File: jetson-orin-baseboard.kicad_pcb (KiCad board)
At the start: 2 copper layers, 0 parts

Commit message: Add basic mechanical outline
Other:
- board outline added: 110 x 55 mm
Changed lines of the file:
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@@
   )
   (net 0 "")
+  (gr_rect (start 20 20) (end 130 75) (layer "Edge.Cuts") (width 0.1) (fill none))
 )

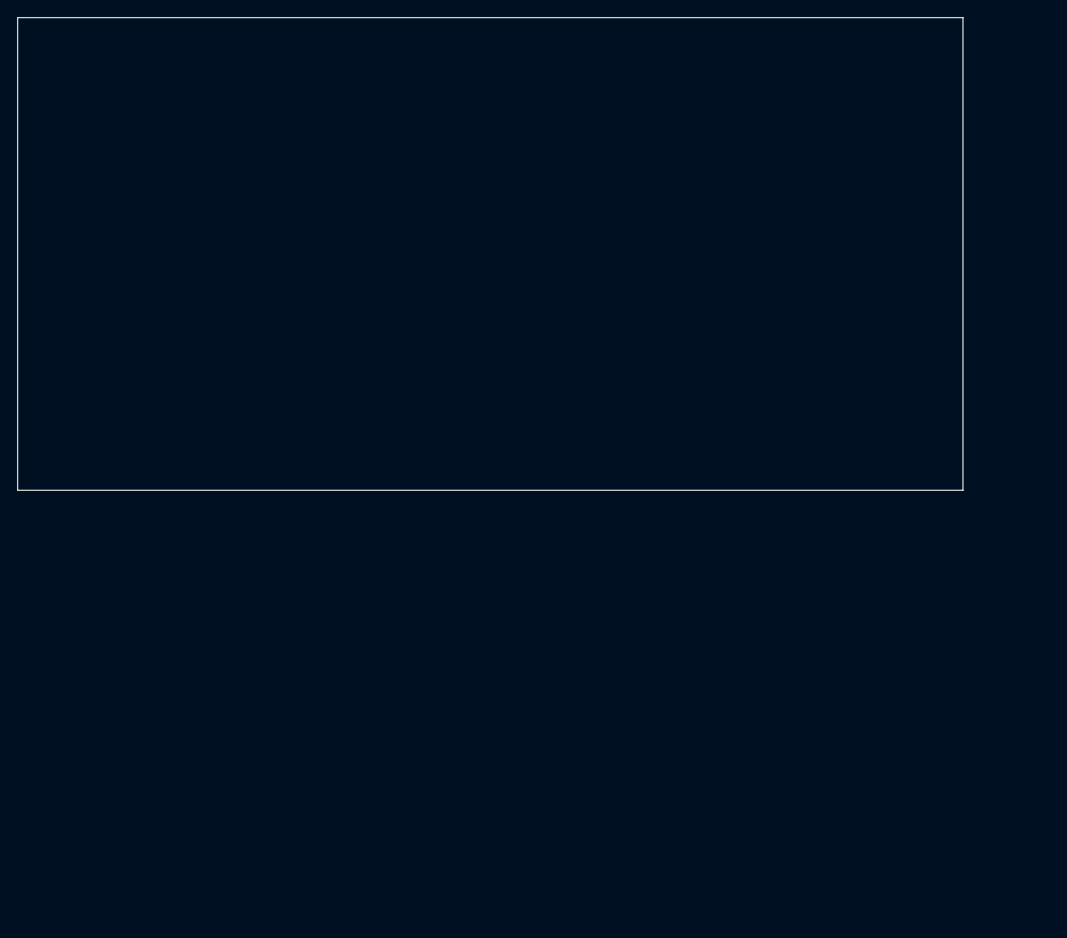
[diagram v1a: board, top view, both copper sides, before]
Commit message: Setup stackup and add stackup table
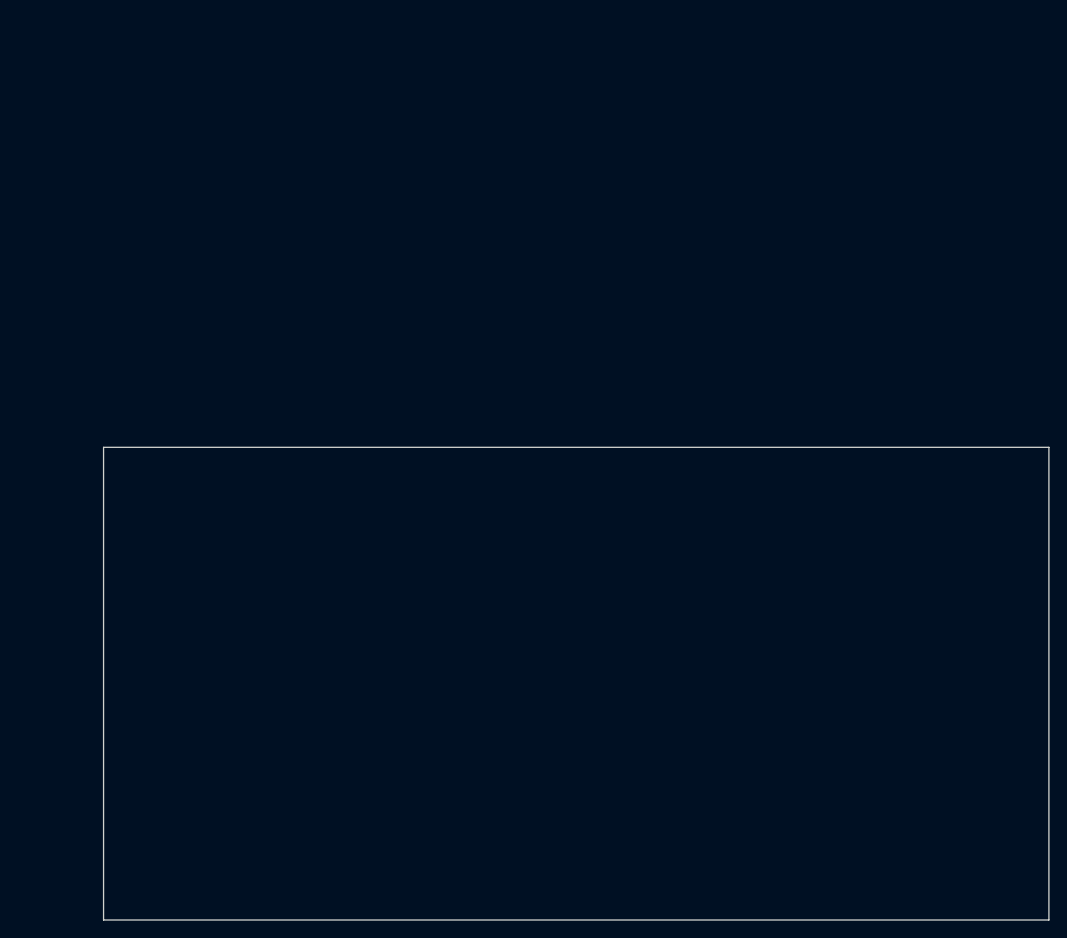
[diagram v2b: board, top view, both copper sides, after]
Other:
- copper layers 2 -> 8
- board text added: "0"
- board text added: "0 mm"
- board text added: "0.01 mm"
- board text added: "0.02"
- board text added: "0.035 mm"
- board text added: "0.12 mm"
- board text added: "0.2 mm"
- board text added: "1"
- board text added: "3.3"
- board text added: "4.3"
- board text added: "4.39"
- board text added: "B.Cu"
- board text added: "B.Mask"
- board text added: "B.Paste"
- board text added: "B.Silkscreen"
- board text added: "Black"
- board text added: "Bottom Silk Screen"
- board text added: "Bottom Solder Mask"
- board text added: "Bottom Solder Paste"
- board text added: "Color"
- board text added: "Dielectric 1"
- board text added: "Dielectric 2"
- board text added: "Dielectric 3 (1/2)"
- board text added: "Dielectric 4"
- board text added: "Dielectric 5 (1/2)"
- board text added: "Dielectric 6"
- board text added: "Dielectric 7"
- board text added: "Epsilon R"
- board text added: "F.Cu"
- board text added: "F.Mask"
- board text added: "F.Paste"
- board text added: "F.Silkscreen"
- board text added: "FR4"
- board text added: "In1.Cu"
- board text added: "In2.Cu"
- board text added: "In3.Cu"
- board text added: "In4.Cu"
- board text added: "In5.Cu"
- board text added: "In6.Cu"
- board text added: "Layer Name"
- board text added: "Loss Tangent"
- board text added: "Material"
- board text added: "Not specified"
- board text added: "PR2116"
- board text added: "Thickness (mm)"
- board text added: "Top Silk Screen"
- board text added: "Top Solder Mask"
- board text added: "Top Solder Paste"
- board text added: "Type"
- board text added: "White"
- board text added: "copper"
- board text added: "core"
- board text added: "prepreg"

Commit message: Initial mechanical arrangement
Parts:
- added BAT201: MS621FE-FL11E, antmicro-footprints:MS621FE-FL11E, F.Cu at (-236.6, 36.6)
- added C201: C_22u_0805_25V, antmicro-footprints:0805-cap, F.Cu at (-316.6, 80.5)
- added C202: C_22u_0805_25V, antmicro-footprints:0805-cap, F.Cu at (-230.2, 29.0)
- added C203: C_22u_0805_25V, antmicro-footprints:0805-cap, F.Cu at (-304.9, 77.2)
- added C204: C_22u_0805_25V, antmicro-footprints:0805-cap, F.Cu at (-316.6, 83.5)
- added C205: C_100n_0402, antmicro-footprints:0402-cap, F.Cu at (-226.3, 28.5)
- added C301: C_10u_0603, antmicro-footprints:0603-cap, F.Cu at (-266.7, 96.3)
- added C302: C_10u_0603, antmicro-footprints:0603-cap, F.Cu at (-270.6, 98.7)
- added C303: C_10u_0603, antmicro-footprints:0603-cap, F.Cu at (-258.5, 89.3)
- added C304: C_10u_0603, antmicro-footprints:0603-cap, F.Cu at (-317.2, 181.8)
- added C305: C_100n_0402, antmicro-footprints:0402-cap, F.Cu at (-258.8, 91.5)
- added C306: C_100n_0402, antmicro-footprints:0402-cap, F.Cu at (-249.4, 89.0)
- added C307: C_100n_0402, antmicro-footprints:0402-cap, F.Cu at (-260.6, 94.1)
- added C308: C_100n_0402, antmicro-footprints:0402-cap, F.Cu at (-270.9, 109.4)
- added C309: C_100n_0402, antmicro-footprints:0402-cap, F.Cu at (-268.0, 106.9)
- added C310: C_100n_0402, antmicro-footprints:0402-cap, F.Cu at (-267.3, 103.0)
- added C311: C_100n_0402, antmicro-footprints:0402-cap, F.Cu at (-263.5, 94.1)
- added C312: C_100n_0402, antmicro-footprints:0402-cap, F.Cu at (-263.5, 96.1)
- added C313: C_100n_0402, antmicro-footprints:0402-cap, F.Cu at (-263.5, 98.1)
- added C318: C_100n_0402, antmicro-footprints:0402-cap, F.Cu at (-270.9, 105.4)
- added C323: C_10u_0603, antmicro-footprints:0603-cap, F.Cu at (-267.0, 98.7)
- added C324: C_10u_0603, antmicro-footprints:0603-cap, F.Cu at (-270.6, 101.2)
- added C401: C_100n_0402, antmicro-footprints:0402-cap, F.Cu at (-128.9, 68.3)
- added C402: C_10u_0603, antmicro-footprints:0603-cap, F.Cu at (-103.0, 31.2)
- added C405: C_10u_0603, antmicro-footprints:0603-cap, F.Cu at (-120.6, 46.8)
- added C412: C_100n_0402, antmicro-footprints:0402-cap, F.Cu at (-110.9, 49.1)
- added C413: C_100n_0402, antmicro-footprints:0402-cap, F.Cu at (-104.7, 41.6)
- added C414: C_100n_0402, antmicro-footprints:0402-cap, F.Cu at (-95.2, 37.0)
- added C415: C_100n_0402, antmicro-footprints:0402-cap, F.Cu at (-117.3, 49.0)
- added C416: C_100n_0402, antmicro-footprints:0402-cap, F.Cu at (-104.5, 33.5)
- added C417: C_100n_0402, antmicro-footprints:0402-cap, F.Cu at (-107.8, 45.6)
- added C418: C_100n_0402, antmicro-footprints:0402-cap, F.Cu at (-87.2, 28.5)
- added C419: C_100n_0402, antmicro-footprints:0402-cap, F.Cu at (-98.1, 35.0)
- added C420: C_100n_0402, antmicro-footprints:0402-cap, F.Cu at (-96.8, 31.0)
- added C421: C_100n_0402, antmicro-footprints:0402-cap, F.Cu at (-111.6, 51.0)
- added C422: C_100n_0402, antmicro-footprints:0402-cap, F.Cu at (-121.8, 56.8)
- added C423: C_100n_0402, antmicro-footprints:0402-cap, F.Cu at (-95.7, 33.0)
- added C424: C_100n_0402, antmicro-footprints:0402-cap, F.Cu at (-99.7, 31.0)
- added C425: C_100n_0402, antmicro-footprints:0402-cap, F.Cu at (-125.4, 62.7)
- added C426: C_100n_0402, antmicro-footprints:0402-cap, F.Cu at (-113.6, 46.0)
- added C427: C_100n_0402, antmicro-footprints:0402-cap, F.Cu at (-128.3, 62.4)
- added C428: C_100n_0402, antmicro-footprints:0402-cap, F.Cu at (-107.8, 47.6)
- added C429: C_100n_0402, antmicro-footprints:0402-cap, F.Cu at (-131.8, 66.0)
- added C430: C_100n_0402, antmicro-footprints:0402-cap, F.Cu at (-90.1, 28.5)
- added C431: C_100n_0402, antmicro-footprints:0402-cap, F.Cu at (-125.4, 60.8)
- added C432: C_100n_0402, antmicro-footprints:0402-cap, F.Cu at (-123.1, 64.7)
- added C433: C_100n_0402, antmicro-footprints:0402-cap, F.Cu at (-93.0, 28.5)
- added C434: C_10u_25V_0603, antmicro-footprints:0603-cap, F.Cu at (-120.6, 49.2)
- added C435: C_10u_0402, antmicro-footprints:0402-cap, F.Cu at (-101.0, 35.5)
- added C436: C_10u_0402, antmicro-footprints:0402-cap, F.Cu at (-117.4, 53.5)
- added C437: C_10u_0402, antmicro-footprints:0402-cap, F.Cu at (-98.9, 41.4)
- added C438: C_10u_0402, antmicro-footprints:0402-cap, F.Cu at (-98.8, 39.4)
- added C439: C_100n_0402, antmicro-footprints:0402-cap, F.Cu at (-110.7, 43.1)
- added C440: C_100n_0402, antmicro-footprints:0402-cap, F.Cu at (-118.9, 55.4)
- added C441: C_100n_0402, antmicro-footprints:0402-cap, F.Cu at (-101.6, 33.5)
- added C442: C_100n_0402, antmicro-footprints:0402-cap, F.Cu at (-128.3, 60.4)
- added C443: C_100n_0402_50V, antmicro-footprints:0402-cap, F.Cu at (-98.1, 37.0)
- added C444: C_100n_0402_50V, antmicro-footprints:0402-cap, F.Cu at (-101.7, 39.4)
- added C501: C_10u_0603, antmicro-footprints:0603-cap, F.Cu at (-32.5, 36.9)
- added C503: C_100n_0402, antmicro-footprints:0402-cap, F.Cu at (-21.7, 40.9)
- added C505: C_100n_0402, antmicro-footprints:0402-cap, F.Cu at (-21.9, 31.0)
- added C507: C_100n_0402, antmicro-footprints:0402-cap, F.Cu at (-33.4, 41.7)
- added C508: C_100n_0402, antmicro-footprints:0402-cap, F.Cu at (-22.8, 37.0)
- added C511: C_100n_0402, antmicro-footprints:0402-cap, F.Cu at (-21.7, 42.9)
- added C512: C_100n_0402, antmicro-footprints:0402-cap, F.Cu at (-10.3, 32.5)
- added C515: C_100n_0402, antmicro-footprints:0402-cap, F.Cu at (-38.0, 52.4)
- added C517: C_10u_0603, antmicro-footprints:0603-cap, F.Cu at (-47.1, 52.4)
- added C519: C_100n_0402, antmicro-footprints:0402-cap, F.Cu at (-24.6, 43.1)
- added C601: C_100n_0805_100V, antmicro-footprints:0805-cap, F.Cu at (-175.4, 50.0)
- added C602: C_10n_0402, antmicro-footprints:0402-cap, F.Cu at (-186.2, 60.3)
- added C603: C_22u_2220_100V, antmicro-footprints:2220-cap, F.Cu at (-190.1, 55.5)
- added C604: C_22u_2220_100V, antmicro-footprints:2220-cap, F.Cu at (-209.6, 85.0)
- added C605: C_22u_2220_100V, antmicro-footprints:2220-cap, F.Cu at (-163.9, 31.0)
- added C606: C_22u_2220_100V, antmicro-footprints:2220-cap, F.Cu at (-173.6, 35.5)
- added C607: C_100n_0402, antmicro-footprints:0402-cap, F.Cu at (-192.9, 68.2)
- added C608: C_47u_16V_1206, antmicro-footprints:1206-cap, F.Cu at (-191.0, 60.6)
- added C609: C_47u_16V_1206, antmicro-footprints:1206-cap, F.Cu at (-174.5, 40.6)
- added C610: C_100n_0402_16V, antmicro-footprints:0402-cap, F.Cu at (-183.3, 60.3)
- added C611: C_100n_0402, antmicro-footprints:0402-cap, F.Cu at (-171.5, 48.2)
- added C701: C_100n_0402, antmicro-footprints:0402-cap, F.Cu at (-91.8, 113.0)
- added C702: C_100n_0402, antmicro-footprints:0402-cap, F.Cu at (-88.9, 115.0)
- added C703: C_100n_0402, antmicro-footprints:0402-cap, F.Cu at (-96.4, 120.0)
- added C704: C_100n_0402, antmicro-footprints:0402-cap, F.Cu at (-124.1, 148.2)
- added C705: C_100n_0402, antmicro-footprints:0402-cap, F.Cu at (-131.8, 158.0)
- added C706: C_100n_0402, antmicro-footprints:0402-cap, F.Cu at (-124.3, 144.2)
- added C707: C_100n_0402, antmicro-footprints:0402-cap, F.Cu at (-117.0, 137.3)
- added C708: C_1u_0402, antmicro-footprints:0402-cap, F.Cu at (-114.1, 139.2)
- added C709: C_1u_0402, antmicro-footprints:0402-cap, F.Cu at (-126.1, 146.2)
- added C710: C_1u_0402, antmicro-footprints:0402-cap, F.Cu at (-112.5, 135.3)
- added C711: C_1u_0402, antmicro-footprints:0402-cap, F.Cu at (-93.5, 117.0)
- added C801: C_100n_0402, antmicro-footprints:0402-cap, F.Cu at (-192.5, 122.6)
- added C802: C_100n_0402, antmicro-footprints:0402-cap, F.Cu at (-210.9, 137.8)
- added C803: C_100n_0402, antmicro-footprints:0402-cap, F.Cu at (-191.4, 120.5)
- added C804: C_100n_0402, antmicro-footprints:0402-cap, F.Cu at (-208.0, 139.8)
- added C805: C_100n_0402, antmicro-footprints:0402-cap, F.Cu at (-208.8, 173.7)
- added C806: C_100n_0402, antmicro-footprints:0402-cap, F.Cu at (-218.1, 184.2)
- added C807: C_100n_0402, antmicro-footprints:0402-cap, F.Cu at (-180.7, 113.0)
- added C808: C_100n_0402, antmicro-footprints:0402-cap, F.Cu at (-191.4, 118.5)
- added C809: C_100n_0402, antmicro-footprints:0402-cap, F.Cu at (-200.4, 134.0)
- added C810: C_100n_0402, antmicro-footprints:0402-cap, F.Cu at (-202.6, 132.0)
- added C811: C_100n_0402, antmicro-footprints:0402-cap, F.Cu at (-202.2, 136.4)
- added C812: C_100n_0402, antmicro-footprints:0402-cap, F.Cu at (-210.9, 141.8)
- added C813: C_100n_0402, antmicro-footprints:0402-cap, F.Cu at (-185.6, 119.4)
- added C901: C_22u_0805_25V, antmicro-footprints:0805-cap, F.Cu at (-120.8, 171.8)
- added C902: C_22u_0805_25V, antmicro-footprints:0805-cap, F.Cu at (-120.8, 174.7)
- added C903: C_10u_0402, antmicro-footprints:0402-cap, F.Cu at (-104.4, 163.2)
- added C904: C_22u_0805_25V, antmicro-footprints:0805-cap, F.Cu at (-112.3, 163.7)
- added C905: C_22u_0805_25V, antmicro-footprints:0805-cap, F.Cu at (-125.8, 179.5)
- added C906: C_22u_0805_25V, antmicro-footprints:0805-cap, F.Cu at (-125.8, 176.6)
- added C907: C_22u_0805_25V, antmicro-footprints:0805-cap, F.Cu at (-131.9, 183.7)
- added C908: C_100n_0402_50V, antmicro-footprints:0402-cap, F.Cu at (-121.1, 183.1)
- added C909: C_100n_0402_50V, antmicro-footprints:0402-cap, F.Cu at (-101.5, 163.2)
- added C910: C_1u_0402, antmicro-footprints:0402-cap, F.Cu at (-121.1, 185.1)
- added C911: C_1u_0402, antmicro-footprints:0402-cap, F.Cu at (-107.2, 173.2)
- added C912: C_10u_0402, antmicro-footprints:0402-cap, F.Cu at (-112.2, 177.2)
- added C913: C_220n_0402, antmicro-footprints:0402-cap, F.Cu at (-109.2, 169.2)
- added C914: C_220n_0402, antmicro-footprints:0402-cap, F.Cu at (-132.9, 186.1)
- added C915: C_100n_0402, antmicro-footprints:0402-cap, F.Cu at (-109.3, 175.2)
- added C916: C_33p_0402, antmicro-footprints:0402-cap, F.Cu at (-124.0, 185.1)
- added C917: C_33p_0402, antmicro-footprints:0402-cap, F.Cu at (-98.6, 165.2)
- added C918: C_22u_0402, antmicro-footprints:0402-cap, F.Cu at (-121.9, 181.1)
- added C919: C_22u_0402, antmicro-footprints:0402-cap, F.Cu at (-109.2, 167.2)
- added C920: C_22u_0402, antmicro-footprints:0402-cap, F.Cu at (-106.3, 167.2)
- added C921: C_22u_0402, antmicro-footprints:0402-cap, F.Cu at (-98.6, 163.2)
- added C922: C_100n_0402, antmicro-footprints:0402-cap, F.Cu at (-124.0, 183.1)
- added C923: C_22u_0402, antmicro-footprints:0402-cap, F.Cu at (-118.2, 183.1)
- added C924: C_22u_0402, antmicro-footprints:0402-cap, F.Cu at (-101.5, 165.2)
- added C925: C_100n_0402, antmicro-footprints:0402-cap, F.Cu at (-113.0, 173.1)
- added C926: C_2u2_0402, antmicro-footprints:0402-cap, F.Cu at (-112.2, 175.2)
- added C927: C_1u_0402, antmicro-footprints:0402-cap, F.Cu at (-115.2, 176.4)
- added D301: KP-1608CGCK, antmicro-footprints:LED_0603, F.Cu at (-270.4, 96.3)
- added D401: LTST-C190GKT, antmicro-footprints:LED_0603, F.Cu at (-117.0, 44.3)
- added D402: LTST-C190GKT, antmicro-footprints:LED_0603, F.Cu at (-128.1, 53.7)
- added D403: LTST-C190GKT, antmicro-footprints:LED_0603, F.Cu at (-102.8, 28.8)
- added D404: LTST-C190GKT, antmicro-footprints:LED_0603, F.Cu at (-120.8, 44.3)
- added D405: LTST-C190GKT, antmicro-footprints:LED_0603, F.Cu at (-128.1, 56.1)
- added D406: DF2S30FS, antmicro-footprints:SOD-923, F.Cu at (-88.3, 30.6)
- added D407: DF2S30FS, antmicro-footprints:SOD-923, F.Cu at (-92.5, 34.6)
- added D408: LTST-C190GKT, antmicro-footprints:LED_0603, F.Cu at (-123.7, 52.1)
- added D501: ESD9X5.0ST5G, antmicro-footprints:SOD-923, F.Cu at (-7.58, 30.6)
- added D503: LTST-C190GKT, antmicro-footprints:LED_0603, F.Cu at (-40.3, 43.8)
- added D601: CD-MMBL110S, antmicro-footprints:DFN3538, F.Cu at (-175.4, 45.4)
- added D602: CD-MMBL110S, antmicro-footprints:DFN3538, F.Cu at (-166.9, 37.6)
- added D603: PTVS58VS1UR,115, antmicro-footprints:SOD-123F, F.Cu at (-202.6, 77.8)
- added D604: KP-1608CGCK, antmicro-footprints:LED_0603, F.Cu at (-192.4, 63.5)
- added D605: PDS760-13, antmicro-footprints:PDS760-13, F.Cu at (-210.2, 78.6)
- added D701: LTST-C190GKT, antmicro-footprints:LED_0603, F.Cu at (-127.1, 137.6)
- added D702: LTST-C190GKT, antmicro-footprints:LED_0603, F.Cu at (-127.7, 142.5)
- added D703: LTST-C190GKT, antmicro-footprints:LED_0603, F.Cu at (-127.7, 140.0)
- added D704: LTST-C190GKT, antmicro-footprints:LED_0603, F.Cu at (-133.1, 147.3)
- added D705: LTST-C190GKT, antmicro-footprints:LED_0603, F.Cu at (-137.1, 148.9)
- added D706: LTST-C190GKT, antmicro-footprints:LED_0603, F.Cu at (-137.1, 151.4)
- added D707: LTST-C190GKT, antmicro-footprints:LED_0603, F.Cu at (-104.3, 124.9)
- added D708: LTST-C190GKT, antmicro-footprints:LED_0603, F.Cu at (-133.3, 149.8)
- added D709: LTST-C190GKT, antmicro-footprints:LED_0603, F.Cu at (-123.3, 137.6)
- added D710: LTST-C190GKT, antmicro-footprints:LED_0603, F.Cu at (-133.1, 144.8)
- added D801: LTST-C190GKT, antmicro-footprints:LED_0603, F.Cu at (-210.4, 135.6)
- added D802: LTST-C190GKT, antmicro-footprints:LED_0603, F.Cu at (-205.7, 129.8)
- added D803: LTST-C190GKT, antmicro-footprints:LED_0603, F.Cu at (-186.9, 113.2)
- added FB201: 74279221100, antmicro-footprints:1206-res, F.Cu at (-315.7, 77.4)
- added FB601: BLM21PG221SN1D, antmicro-footprints:0805-res, F.Cu at (-170.5, 43.7)
- added FB602: BLM21PG221SN1D, antmicro-footprints:0805-res, F.Cu at (-162.1, 35.9)
- added IC601: ACPL-217-500E, antmicro-footprints:SOIC127P700X242-4N, F.Cu at (-173.0, 29.8)
- added IC901: TPS7A0518PDBVT, antmicro-footprints:SOT-23-5, F.Cu at (-117.1, 164.8)
- added J1: WE_685119136923, antmicro-footprints:WE_685119136923, F.Cu at (113.5, 121.0)
- added J2: 52991-0508, antmicro-footprints:529910508, F.Cu at (136.0, 96.0)
- added J301: 1-2199230-6, antmicro-footprints:1-2199230-6, B.Cu at (121.5, 86.0)
- added J302: 2199230-6, antmicro-footprints:2199230-4, B.Cu at (121.5, 109.0)
- added J401: USB4105-GF-A, antmicro-footprints:GCT_USB4105-GF-A, F.Cu at (53.0, 122.5)
- added J402: WE_632723300011_alt_symbol, antmicro-footprints:WE_632723300011, F.Cu at (75.0, 119.0)
- added J501: WE_632723300011_alt_symbol, antmicro-footprints:WE_632723300011, F.Cu at (95.0, 119.0)
- added J601: 5-2337992-8, antmicro-footprints:5-2337992-8, F.Cu at (32.3, 105.1)
- added J701: WE_68715014522, antmicro-footprints:WE_68715014522, B.Cu at (134.5, 96.5)
- added J702: WE_68715014522, antmicro-footprints:WE_68715014522, B.Cu at (91.0, 75.3)
- added J801: TC2050-IDC-NL, antmicro-footprints:TC2050-IDC-NL_2x05_Vertical, F.Cu at (-212.8, 168.7)
- added J803: 533980471, antmicro-footprints:Molex_PicoBlade_53398-0471_1x04-1MP_P1.25mm_Vertical, F.Cu at (-205.8, 114.9)
- added L901: IHLP2525CZER2R2M01, antmicro-footprints:IHLP2525CZER, F.Cu at (-124.3, 166.3)
- added L902: IHLP2525CZER2R2M01, antmicro-footprints:IHLP2525CZER, F.Cu at (-134.2, 173.1)
- added M1: ~, antmicro-footprints:jetson-nano-connector, F.Cu at (124.8, 119.4)
- added M1: M2_4222, antmicro-footprints:m2_4222, B.Cu at (81.5, 109.0)
- added M301: M2_2280, antmicro-footprints:m2_2280, B.Cu at (43.1, 86.0)
- added Q401: BSS138W-7-F, antmicro-footprints:SOT-323, F.Cu at (-114.7, 38.5)
- added Q402: BSS138W-7-F, antmicro-footprints:SOT-323, F.Cu at (-106.8, 29.6)
- added Q501: BSS138W-7-F, antmicro-footprints:SOT-323, F.Cu at (-46.9, 49.1)
- added Q701: BSS138W-7-F, antmicro-footprints:SOT-323, F.Cu at (-137.0, 145.6)
- added Q702: BSS138W-7-F, antmicro-footprints:SOT-323, F.Cu at (-123.0, 134.3)
- added Q703: BSS138W-7-F, antmicro-footprints:SOT-323, F.Cu at (-118.9, 134.3)
- added Q704: BSS138W-7-F, antmicro-footprints:SOT-323, F.Cu at (-127.0, 134.3)
- added Q801: BSS138W-7-F, antmicro-footprints:SOT-323, F.Cu at (-206.0, 126.5)
- added Q802: BSS138W-7-F, antmicro-footprints:SOT-323, F.Cu at (-217.5, 181.1)
- added Q803: BSS138W-7-F, antmicro-footprints:SOT-323, F.Cu at (-201.9, 126.5)
- added Q804: BSS138W-7-F, antmicro-footprints:SOT-323, F.Cu at (-194.8, 119.5)
- added Q901: BSS138W-7-F, antmicro-footprints:SOT-323, F.Cu at (-107.9, 164.2)
- added Q902: BSS138W-7-F, antmicro-footprints:SOT-323, F.Cu at (-116.3, 169.5)
- added Q903: BSS138W-7-F, antmicro-footprints:SOT-323, F.Cu at (-127.5, 184.2)
- added R1: R_0R_0402, antmicro-footprints:0402-res, F.Cu at (-255.3, 89.0)
- added R2: R_0R_0402, antmicro-footprints:0402-res, F.Cu at (-270.9, 107.4)
- added R201: R_0R_0402, antmicro-footprints:0402-res, F.Cu at (-312.7, 81.8)
- added R202: R_0R_0402, antmicro-footprints:0402-res, F.Cu at (-305.9, 79.7)
- added R203: R_0R_0402, antmicro-footprints:0402-res, F.Cu at (-301.0, 76.7)
- added R204: R_10k_0402, antmicro-footprints:0402-res, F.Cu at (-312.7, 83.8)
- added R205: R_0R_0402, antmicro-footprints:0402-res, F.Cu at (-304.0, 81.6)
- added R206: R_0R_0402, antmicro-footprints:0402-res, F.Cu at (-306.9, 83.8)
- added R207: R_0R_0402, antmicro-footprints:0402-res, F.Cu at (-309.8, 81.8)
- added R208: R_0R_0402, antmicro-footprints:0402-res, F.Cu at (-239.1, 43.9)
- added R209: R_0R_0402, antmicro-footprints:0402-res, F.Cu at (-306.9, 81.8)
- added R210: R_0R_0402, antmicro-footprints:0402-res, F.Cu at (-303.0, 79.7)
- added R211: R_0R_0402, antmicro-footprints:0402-res, F.Cu at (-298.1, 76.7)
- added R212: R_0R_0402, antmicro-footprints:0402-res, F.Cu at (-309.8, 83.8)
- added R301: R_10k_0402, antmicro-footprints:0402-res, F.Cu at (-294.4, 171.5)
- added R302: R_10k_0402, antmicro-footprints:0402-res, F.Cu at (-294.4, 144.6)
- added R303: R_10k_0402, antmicro-footprints:0402-res, F.Cu at (-264.4, 101.0)
- added R304: R_0R_0402, antmicro-footprints:0402-res, F.Cu at (-255.9, 91.5)
- added R305: R_0R_0402, antmicro-footprints:0402-res, F.Cu at (-267.3, 101.0)
- added R306: R_0R_0402, antmicro-footprints:0402-res, F.Cu at (-260.6, 96.1)
- added R307: R_330R_0603, antmicro-footprints:0603-res, F.Cu at (-289.0, 139.8)
- added R308: R_0R_0402, antmicro-footprints:0402-res, F.Cu at (-257.6, 93.5)
- added R309: R_0R_0402, antmicro-footprints:0402-res, F.Cu at (-252.4, 89.0)
- added R312: R_10k_0402, antmicro-footprints:0402-res, F.Cu at (-253.0, 91.0)
- added R313: R_10k_0402, antmicro-footprints:0402-res, F.Cu at (-270.9, 103.4)
- added R316: R_0R_0402, antmicro-footprints:0402-res, F.Cu at (-268.0, 105.0)
- added R401: R_0R_0402, antmicro-footprints:0402-res, F.Cu at (-119.5, 59.4)
- added R402: R_10k_0402, antmicro-footprints:0402-res, F.Cu at (-126.0, 68.7)
- added R403: R_100k_0402, antmicro-footprints:0402-res, F.Cu at (-117.4, 51.5)
- added R404: R_10k_0402, antmicro-footprints:0402-res, F.Cu at (-101.0, 37.4)
- added R405: R_100k_0402, antmicro-footprints:0402-res, F.Cu at (-95.2, 35.0)
- added R406: R_0R_0402, antmicro-footprints:0402-res, F.Cu at (-104.8, 43.6)
- added R407: R_0R_0402, antmicro-footprints:0402-res, F.Cu at (-124.7, 56.8)
- added R408: R_0R_0402, antmicro-footprints:0402-res, F.Cu at (-111.6, 53.0)
- added R409: R_0R_0402, antmicro-footprints:0402-res, F.Cu at (-98.7, 33.0)
- added R410: R_0R_0402, antmicro-footprints:0402-res, F.Cu at (-128.9, 64.3)
- added R411: R_0R_0402, antmicro-footprints:0402-res, F.Cu at (-95.9, 28.5)
- added R417: R_0R_0402, antmicro-footprints:0402-res, F.Cu at (-89.9, 32.5)
- added R418: R_0R_0402, antmicro-footprints:0402-res, F.Cu at (-107.6, 41.6)
- added R419: R_0R_0402, antmicro-footprints:0402-res, F.Cu at (-107.5, 39.7)
- added R420: R_0R_0402, antmicro-footprints:0402-res, F.Cu at (-120.3, 51.5)
- added R421: R_0R_0402, antmicro-footprints:0402-res, F.Cu at (-113.6, 44.0)
- added R422: R_200R_0603, antmicro-footprints:0603-res, F.Cu at (-110.9, 40.9)
- added R423: R_200R_0603, antmicro-footprints:0603-res, F.Cu at (-131.5, 61.8)
- added R424: R_0R_0402, antmicro-footprints:0402-res, F.Cu at (-116.0, 57.4)
- added R425: R_0R_0402, antmicro-footprints:0402-res, F.Cu at (-128.9, 70.3)
- added R426: R_200R_0603, antmicro-footprints:0603-res, F.Cu at (-99.1, 28.8)
- added R427: R_200R_0603, antmicro-footprints:0603-res, F.Cu at (-124.4, 54.5)
- added R428: R_10k_0402, antmicro-footprints:0402-res, F.Cu at (-110.7, 47.1)
- added R429: R_0R_0402, antmicro-footprints:0402-res, F.Cu at (-126.0, 64.7)
- added R430: R_0R_0402, antmicro-footprints:0402-res, F.Cu at (-113.8, 48.0)
- added R431: R_0R_0402, antmicro-footprints:0402-res, F.Cu at (-131.8, 72.0)
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
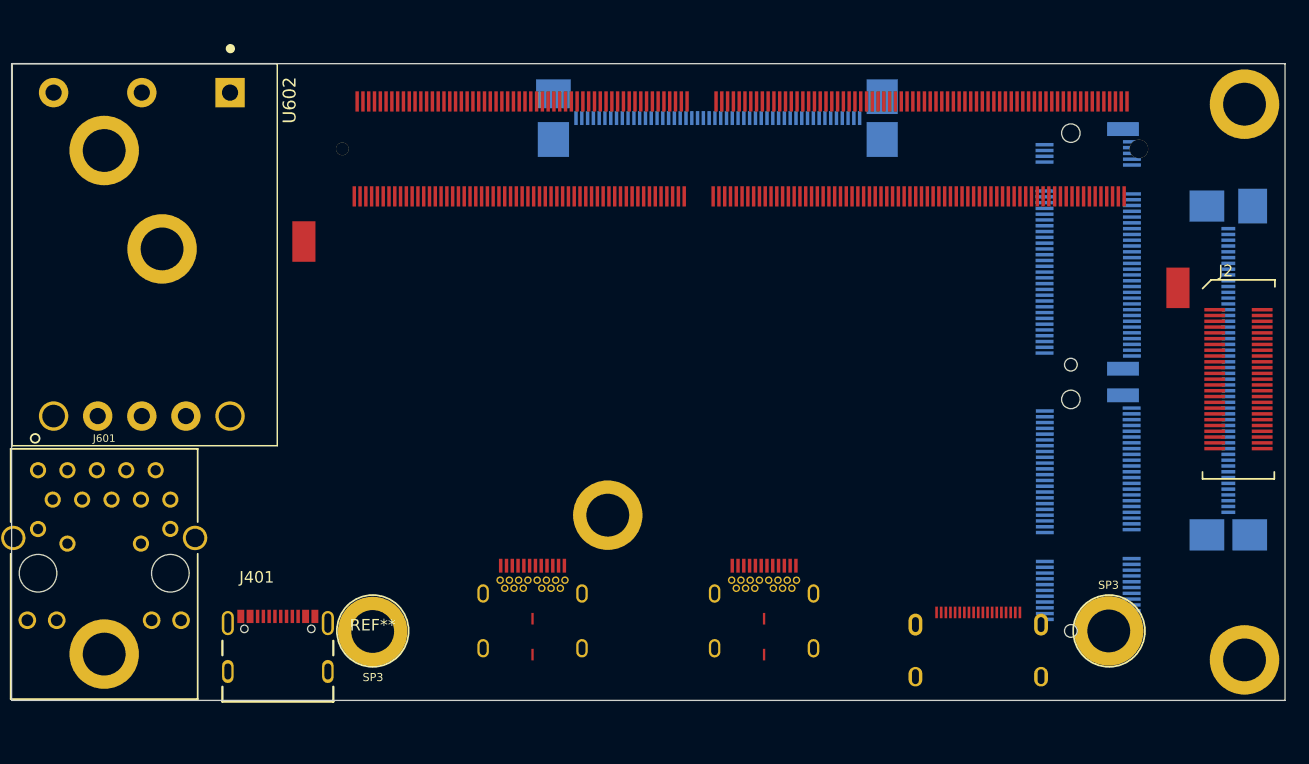
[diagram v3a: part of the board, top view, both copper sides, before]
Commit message: Move M.2 key E under SoM
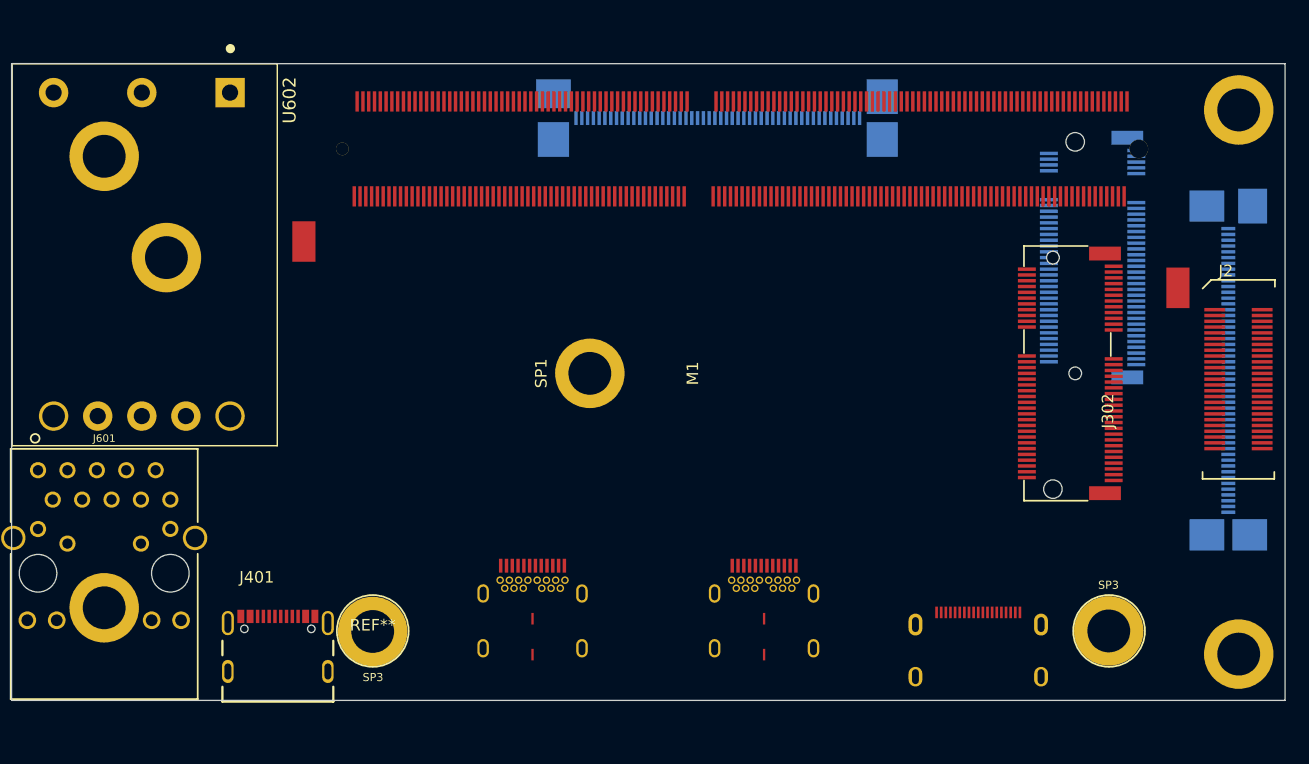
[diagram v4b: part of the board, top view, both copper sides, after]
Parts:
- J302, M1, SP1: moved to F.Cu
- moved J302 12.3 mm to (120.0, 96.8), turned to -90 degrees
- moved M1 12.3 mm to (80.0, 96.8), turned to -90 degrees
- moved SP1 12.3 mm to (80.0, 96.8), turned to 90 degrees
- moved SP3 4.00 mm to (38.0, 117.0)
- moved J301 0.84 mm to (121.9, 86.8)
- moved M301 0.84 mm to (43.5, 86.8)
- moved SP301 0.84 mm to (43.4, 86.8)
- moved SP2 0.71 mm to (136.0, 121.0)
- moved SP4 0.71 mm to (136.0, 74.0)
- moved SP5 0.50 mm to (38.0, 78.0)

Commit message: Update expansion connector symbol, iport it to PCB
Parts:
- removed C801, C802, C803, C805, C806, C807, C811, C813: C_100n_0402, antmicro-footprints:0402-cap
- removed J2: 52991-0508, antmicro-footprints:529910508
- removed R801, R805, R810: R_0R_0402, antmicro-footprints:0402-res
- removed REF**: compute-module-4, antmicro-footprints:jetson-xavier-nx-module-5.2H
- removed the SP3 at (124.8, 119.0)
- removed the SP3 at (61.2, 119.0)
- removed U801, U802, U804: TXB0108DQSR, antmicro-footprints:USON-20_2x4mm_P0.4mm
- added C1: C_100n_0402, antmicro-footprints:0402-cap, F.Cu at (41.9, 230.1)
- added C2: C_100n_0402, antmicro-footprints:0402-cap, F.Cu at (48.1, 224.0)
- added C3: C_100n_0402, antmicro-footprints:0402-cap, F.Cu at (48.1, 226.0)
- added C4: C_100n_0402, antmicro-footprints:0402-cap, F.Cu at (45.2, 224.0)
- added C5: C_100n_0402, antmicro-footprints:0402-cap, F.Cu at (41.9, 228.1)
- added C6: C_100n_0402, antmicro-footprints:0402-cap, F.Cu at (45.2, 226.0)
- added C7: C_100n_0402, antmicro-footprints:0402-cap, F.Cu at (47.7, 228.0)
- added C8: C_100n_0402, antmicro-footprints:0402-cap, F.Cu at (44.8, 228.1)
- added R3: R_0R_0402, antmicro-footprints:0402-res, F.Cu at (41.9, 232.1)
- added R4: R_0R_0402, antmicro-footprints:0402-res, F.Cu at (44.8, 230.1)
- added U1: TPD6F003, Package_SON:Texas_R-PWSON-N12_EP0.4x2mm, F.Cu at (43.0, 188.5)
- J1: value WE_685119136923 -> ERF8-040-05.0-L-DV-K-TR; footprint antmicro-footprints:WE_685119136923 -> antmicro-footprints:ERF8-XXX-XX.X-X-DV-XXXX-TR
- moved J1 68.7 mm to (64.4, 169.0)
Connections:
- net /USB Debug, DP, Hub/DP1_AUX_C_N renamed /USB Debug, DP/DP1_AUX_C_N
- net /USB Debug, DP, Hub/DP1_AUX_C_P renamed /USB Debug, DP/DP1_AUX_C_P
- net /USB Debug, DP, Hub/DP1_TXD0_C_N renamed /USB Debug, DP/DP1_TXD0_C_N
- net /USB Debug, DP, Hub/DP1_TXD0_C_P renamed /USB Debug, DP/DP1_TXD0_C_P
- net /USB Debug, DP, Hub/DP1_TXD1_C_N renamed /USB Debug, DP/DP1_TXD1_C_N
- net /USB Debug, DP, Hub/DP1_TXD1_C_P renamed /USB Debug, DP/DP1_TXD1_C_P
- net /USB Debug, DP, Hub/DP1_TXD2_C_N renamed /USB Debug, DP/DP1_TXD2_C_N
- net /USB Debug, DP, Hub/DP1_TXD2_C_P renamed /USB Debug, DP/DP1_TXD2_C_P
- net /USB Debug, DP, Hub/DP1_TXD3_C_N renamed /USB Debug, DP/DP1_TXD3_C_N
- net /USB Debug, DP, Hub/DP1_TXD3_C_P renamed /USB Debug, DP/DP1_TXD3_C_P
- net /USB Debug, DP, Hub/DRAIN1 renamed /USB Debug, DP/DRAIN1
- net /USB Debug, DP, Hub/DRAIN2 renamed /USB Debug, DP/DRAIN2
- net /USB Debug, DP, Hub/FLASH_CLK renamed /USB Debug, DP/FLASH_CLK
- net /USB Debug, DP, Hub/FLASH_MISO renamed /USB Debug, DP/FLASH_MISO
- net /USB Debug, DP, Hub/FLASH_MOSI renamed /USB Debug, DP/FLASH_MOSI
- net /USB Debug, DP, Hub/FTDI_3V3 renamed /USB Debug, DP/FTDI_3V3
- net /USB Debug, DP, Hub/FTDI_CBUS0 renamed /USB Debug, DP/FTDI_CBUS0
- net /USB Debug, DP, Hub/FTDI_CBUS3 renamed /USB Debug, DP/FTDI_CBUS3
- net /USB Debug, DP, Hub/FTDI_LED_RX renamed /USB Debug, DP/FTDI_LED_RX
- net /USB Debug, DP, Hub/FTDI_LED_TX renamed /USB Debug, DP/FTDI_LED_TX
- net /USB Debug, DP, Hub/PDC_ADCIN1 renamed /USB Debug, DP/PDC_ADCIN1
- net /USB Debug, DP, Hub/PDC_ADCIN2 renamed /USB Debug, DP/PDC_ADCIN2
- net /USB Debug, DP, Hub/PDC_CTL0 renamed /USB Debug, DP/PDC_CTL0
- net /USB Debug, DP, Hub/PDC_CTL1 renamed /USB Debug, DP/PDC_CTL1
- net /USB Debug, DP, Hub/PDC_FLIP renamed /USB Debug, DP/PDC_FLIP
- net /USB Debug, DP, Hub/PDC_GPIO14 renamed /USB Debug, DP/PDC_GPIO14
- net /USB Debug, DP, Hub/PDC_GPIO15 renamed /USB Debug, DP/PDC_GPIO15
- net /USB Debug, DP, Hub/PDC_I2C1_IRQn renamed /USB Debug, DP/PDC_I2C1_IRQn
- net /USB Debug, DP, Hub/PDC_I2C1_SCL renamed /USB Debug, DP/PDC_I2C1_SCL
- net /USB Debug, DP, Hub/PDC_I2C1_SDA renamed /USB Debug, DP/PDC_I2C1_SDA
- net /USB Debug, DP, Hub/PDC_I2C2_IRQn renamed /USB Debug, DP/PDC_I2C2_IRQn
- net /USB Debug, DP, Hub/PDC_I2C2_SCL renamed /USB Debug, DP/PDC_I2C2_SCL
- net /USB Debug, DP, Hub/PDC_I2C2_SDA renamed /USB Debug, DP/PDC_I2C2_SDA
- net /USB Debug, DP, Hub/PDC_I2C3_SCL renamed /USB Debug, DP/PDC_I2C3_SCL
- net /USB Debug, DP, Hub/PDC_I2C3_SDA renamed /USB Debug, DP/PDC_I2C3_SDA
- net /USB Debug, DP, Hub/PDC_LDO_1V8 renamed /USB Debug, DP/PDC_LDO_1V8
- net /USB Debug, DP, Hub/PDC_LDO_3V3 renamed /USB Debug, DP/PDC_LDO_3V3
- net /USB Debug, DP, Hub/PDC_RESET renamed /USB Debug, DP/PDC_RESET
- net /USB Debug, DP, Hub/USBC0_CC1 renamed /USB Debug, DP/USBC0_CC1
- net /USB Debug, DP, Hub/USBC0_CC2 renamed /USB Debug, DP/USBC0_CC2
- net /USB Debug, DP, Hub/USBC0_CONN_RX1_N renamed /USB Debug, DP/USBC0_CONN_RX1_N
- net /USB Debug, DP, Hub/USBC0_CONN_RX1_P renamed /USB Debug, DP/USBC0_CONN_RX1_P
- net /USB Debug, DP, Hub/USBC0_CONN_RX2_N renamed /USB Debug, DP/USBC0_CONN_RX2_N
- net /USB Debug, DP, Hub/USBC0_CONN_RX2_P renamed /USB Debug, DP/USBC0_CONN_RX2_P
- net /USB Debug, DP, Hub/USBC0_CONN_TX1_N renamed /USB Debug, DP/USBC0_CONN_TX1_N
- net /USB Debug, DP, Hub/USBC0_CONN_TX1_P renamed /USB Debug, DP/USBC0_CONN_TX1_P
- net /USB Debug, DP, Hub/USBC0_CONN_TX2_N renamed /USB Debug, DP/USBC0_CONN_TX2_N
- net /USB Debug, DP, Hub/USBC0_CONN_TX2_P renamed /USB Debug, DP/USBC0_CONN_TX2_P
- net /USB Debug, DP, Hub/USBC0_CTL0 renamed /USB Debug, DP/USBC0_CTL0
- net /USB Debug, DP, Hub/USBC0_CTL1 renamed /USB Debug, DP/USBC0_CTL1
- net /USB Debug, DP, Hub/USBC0_DPEQ0 renamed /USB Debug, DP/USBC0_DPEQ0
- net /USB Debug, DP, Hub/USBC0_DPEQ1 renamed /USB Debug, DP/USBC0_DPEQ1
- net /USB Debug, DP, Hub/USBC0_EQ0 renamed /USB Debug, DP/USBC0_EQ0
- net /USB Debug, DP, Hub/USBC0_EQ1 renamed /USB Debug, DP/USBC0_EQ1
- net /USB Debug, DP, Hub/USBC0_FLIP renamed /USB Debug, DP/USBC0_FLIP
- net /USB Debug, DP, Hub/USBC0_I2C_EN renamed /USB Debug, DP/USBC0_I2C_EN
- net /USB Debug, DP, Hub/USBC0_RX1_N renamed /USB Debug, DP/USBC0_RX1_N
- net /USB Debug, DP, Hub/USBC0_RX1_P renamed /USB Debug, DP/USBC0_RX1_P
- net /USB Debug, DP, Hub/USBC0_RX2_N renamed /USB Debug, DP/USBC0_RX2_N
- net /USB Debug, DP, Hub/USBC0_RX2_P renamed /USB Debug, DP/USBC0_RX2_P
- net /USB Debug, DP, Hub/USBC0_SBU1 renamed /USB Debug, DP/USBC0_SBU1
- net /USB Debug, DP, Hub/USBC0_SBU2 renamed /USB Debug, DP/USBC0_SBU2
- net /USB Debug, DP, Hub/USBC0_SSEQ0 renamed /USB Debug, DP/USBC0_SSEQ0
- net /USB Debug, DP, Hub/USBC0_SSEQ1 renamed /USB Debug, DP/USBC0_SSEQ1
- net /USB Debug, DP, Hub/USBC0_TX1_N renamed /USB Debug, DP/USBC0_TX1_N
- net /USB Debug, DP, Hub/USBC0_TX1_P renamed /USB Debug, DP/USBC0_TX1_P
- net /USB Debug, DP, Hub/USBC0_TX2_N renamed /USB Debug, DP/USBC0_TX2_N
- net /USB Debug, DP, Hub/USBC0_TX2_P renamed /USB Debug, DP/USBC0_TX2_P
- net /USB Debug, DP, Hub/USBC0_VBUS renamed /USB Debug, DP/USBC0_VBUS
- net /USB Debug, DP, Hub/USBC3_CC1 renamed /USB Debug, DP/USBC3_CC1
- net /USB Debug, DP, Hub/USBC3_CC2 renamed /USB Debug, DP/USBC3_CC2
- net /USB Debug, DP, Hub/USBC3_D_N renamed /USB Debug, DP/USBC3_D_N
- net /USB Debug, DP, Hub/USBC3_VBUS renamed /USB Debug, DP/USBC3_VBUS
- net /USB Debug, DP, Hub/USBSS0_RX_C_N renamed /USB Debug, DP/USBSS0_RX_C_N
- net /USB Debug, DP, Hub/USBSS0_RX_C_P renamed /USB Debug, DP/USBSS0_RX_C_P
- net /USB Debug, DP, Hub/USBSS0_TX_C_N renamed /USB Debug, DP/USBSS0_TX_C_N
- net /USB Debug, DP, Hub/USBSS0_TX_C_P renamed /USB Debug, DP/USBSS0_TX_C_P
- net /USB Debug, DP, Hub/USB_FTDI_N renamed /USB Debug, DP/USB_FTDI_N
- net /USB Debug, DP, Hub/USB_FTDI_P renamed /USB Debug, DP/USB_FTDI_P
- net /USB Debug, DP, Hub/~{PFLASH_CS} renamed /USB Debug, DP/~{PFLASH_CS}
- net /USB Debug, DP, Hub/~{PFLASH_HOLD} renamed /USB Debug, DP/~{PFLASH_HOLD}
- net /USB Debug, DP, Hub/~{PFLASH_WP} renamed /USB Debug, DP/~{PFLASH_WP}
- net /USB3 x2/USBC1_ADDR renamed /USB3/USBC1_ADDR
- net /USB3 x2/USBC1_CC1 renamed /USB3/USBC1_CC1
- net /USB3 x2/USBC1_CC2 renamed /USB3/USBC1_CC2
- net /USB3 x2/USBC1_CONN_D_N renamed /USB3/USBC1_CONN_D_N
- net /USB3 x2/USBC1_CONN_D_P renamed /USB3/USBC1_CONN_D_P
- net /USB3 x2/USBC1_CONN_RX1_N renamed /USB3/USBC1_CONN_RX1_N
- net /USB3 x2/USBC1_CONN_RX1_P renamed /USB3/USBC1_CONN_RX1_P
- net /USB3 x2/USBC1_CONN_RX2_N renamed /USB3/USBC1_CONN_RX2_N
- net /USB3 x2/USBC1_CONN_RX2_P renamed /USB3/USBC1_CONN_RX2_P
- net /USB3 x2/USBC1_CONN_TX1_N renamed /USB3/USBC1_CONN_TX1_N
- net /USB3 x2/USBC1_CONN_TX1_P renamed /USB3/USBC1_CONN_TX1_P
- net /USB3 x2/USBC1_CONN_TX2_N renamed /USB3/USBC1_CONN_TX2_N
- net /USB3 x2/USBC1_CONN_TX2_P renamed /USB3/USBC1_CONN_TX2_P
- net /USB3 x2/USBC1_DIR renamed /USB3/USBC1_DIR
- net /USB3 x2/USBC1_FAULT_N renamed /USB3/USBC1_FAULT_N
- net /USB3 x2/USBC1_I2C_SDA renamed /USB3/USBC1_I2C_SDA
- net /USB3 x2/USBC1_ID renamed /USB3/USBC1_ID
- net /USB3 x2/USBC1_ISC_SCL renamed /USB3/USBC1_ISC_SCL
- net /USB3 x2/USBC1_ISET renamed /USB3/USBC1_ISET
- net /USB3 x2/USBC1_I_MODE renamed /USB3/USBC1_I_MODE
- net /USB3 x2/USBC1_PORT renamed /USB3/USBC1_PORT
- net /USB3 x2/USBC1_RX1_N renamed /USB3/USBC1_RX1_N
- net /USB3 x2/USBC1_RX1_P renamed /USB3/USBC1_RX1_P
- net /USB3 x2/USBC1_RX2_N renamed /USB3/USBC1_RX2_N
- net /USB3 x2/USBC1_RX2_P renamed /USB3/USBC1_RX2_P
- net /USB3 x2/USBC1_TX1_N renamed /USB3/USBC1_TX1_N
- net /USB3 x2/USBC1_TX1_P renamed /USB3/USBC1_TX1_P
- net /USB3 x2/USBC1_TX2_N renamed /USB3/USBC1_TX2_N
- net /USB3 x2/USBC1_TX2_P renamed /USB3/USBC1_TX2_P
- net /USB3 x2/USBC1_VBUS renamed /USB3/USBC1_VBUS
- net /USB3 x2/USBC1_VBUS_DET renamed /USB3/USBC1_VBUS_DET
- net /USB3 x2/USBSS1_RX_C_N renamed /USB3/USBSS1_RX_C_N
- net /USB3 x2/USBSS1_RX_C_P renamed /USB3/USBSS1_RX_C_P
- net /USB3 x2/USBSS1_TX_C_N renamed /USB3/USBSS1_TX_C_N
- net /USB3 x2/USBSS1_TX_C_P renamed /USB3/USBSS1_TX_C_P
- net /USB3 x2/~{USBC1_EN_CC} renamed /USB3/~{USBC1_EN_CC}
- net /USB3 x2/~{USBC1_EN_MUX} renamed /USB3/~{USBC1_EN_MUX}
- net /USB3 x2/~{USBC1_INT} renamed /USB3/~{USBC1_INT}
- net Net-(J401-PadA6) renamed /USB Debug, DP/USBC3_D_P
- J1 pad 1: unconnected-(J1-Pad1) -> GND
- J1 pad 10: unconnected-(J1-Pad10) -> GND
- J1 pad 11: unconnected-(J1-Pad11) -> Net-(C6-Pad2)
- J1 pad 12: unconnected-(J1-Pad12) -> Net-(C3-Pad2)
- J1 pad 13: unconnected-(J1-Pad13) -> GND
- J1 pad 14: unconnected-(J1-Pad14) -> Net-(C4-Pad2)
- J1 pad 15: unconnected-(J1-Pad15) -> PCIE2_CLK_N
- J1 pad 16: unconnected-(J1-Pad16) -> GND
- J1 pad 17: unconnected-(J1-Pad17) -> PCIE2_CLK_P
- J1 pad 18: unconnected-(J1-Pad18) -> PCIE3_CLK_N
- J1 pad 19: unconnected-(J1-Pad19) -> GND
- J1 pad 2: unconnected-(J1-Pad2) -> 3V3_STDB
- J1 pad 3: unconnected-(J1-Pad3) -> PCIE2_RX0_N
- J1 pad 4: unconnected-(J1-Pad4) -> GND
- J1 pad 5: unconnected-(J1-Pad5) -> PCIE2_RX0_P
- J1 pad 6: unconnected-(J1-Pad6) -> PCIE2_RX1_N
- J1 pad 7: unconnected-(J1-Pad7) -> GND
- J1 pad 8: unconnected-(J1-Pad8) -> PCIE2_RX1_P
- J1 pad 9: unconnected-(J1-Pad9) -> Net-(C2-Pad2)
- U803 pad 10: unconnected-(U803-Pad10) -> /Peripherals/EXT_GPIO0
- U803 pad 11: unconnected-(U803-Pad11) -> /Peripherals/EXT_GPIO1
- U803 pad 12: unconnected-(U803-Pad12) -> /Peripherals/EXT_GPIO2
- U803 pad 13: unconnected-(U803-Pad13) -> /Peripherals/EXT_GPIO3
- U803 pad 14: unconnected-(U803-Pad14) -> /Peripherals/EXT_GPIO4
- U803 pad 15: unconnected-(U803-Pad15) -> /Peripherals/EXT_GPIO5
